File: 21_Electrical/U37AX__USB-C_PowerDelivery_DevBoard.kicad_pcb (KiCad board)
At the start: 2 copper layers, 96.6 x 80 mm, 93 parts, among them J1 USB_C_Receptacle_USB2.0_16P, J2 USB 2.0 OUT, J3 SWD1, J5 PD VBUS, J6 PD GND, J7 PD OUTPUT, J8 Conn_01x07_Pin, J9 Conn_02x04_Odd_Even, SW1 BTN, SW2 BOOT0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

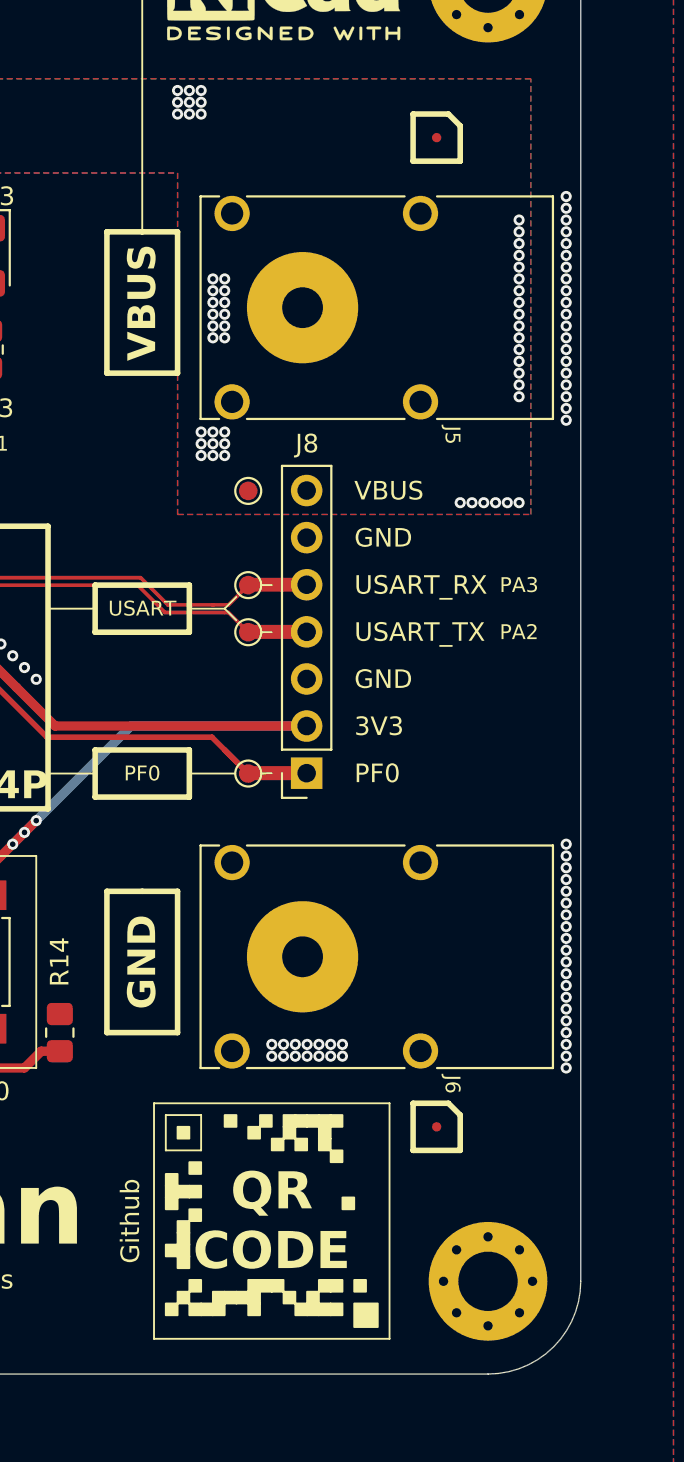
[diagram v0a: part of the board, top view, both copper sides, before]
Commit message: Qr_Code creation, Qr_Code footprint creation, adding Qr_Code to the PCB project
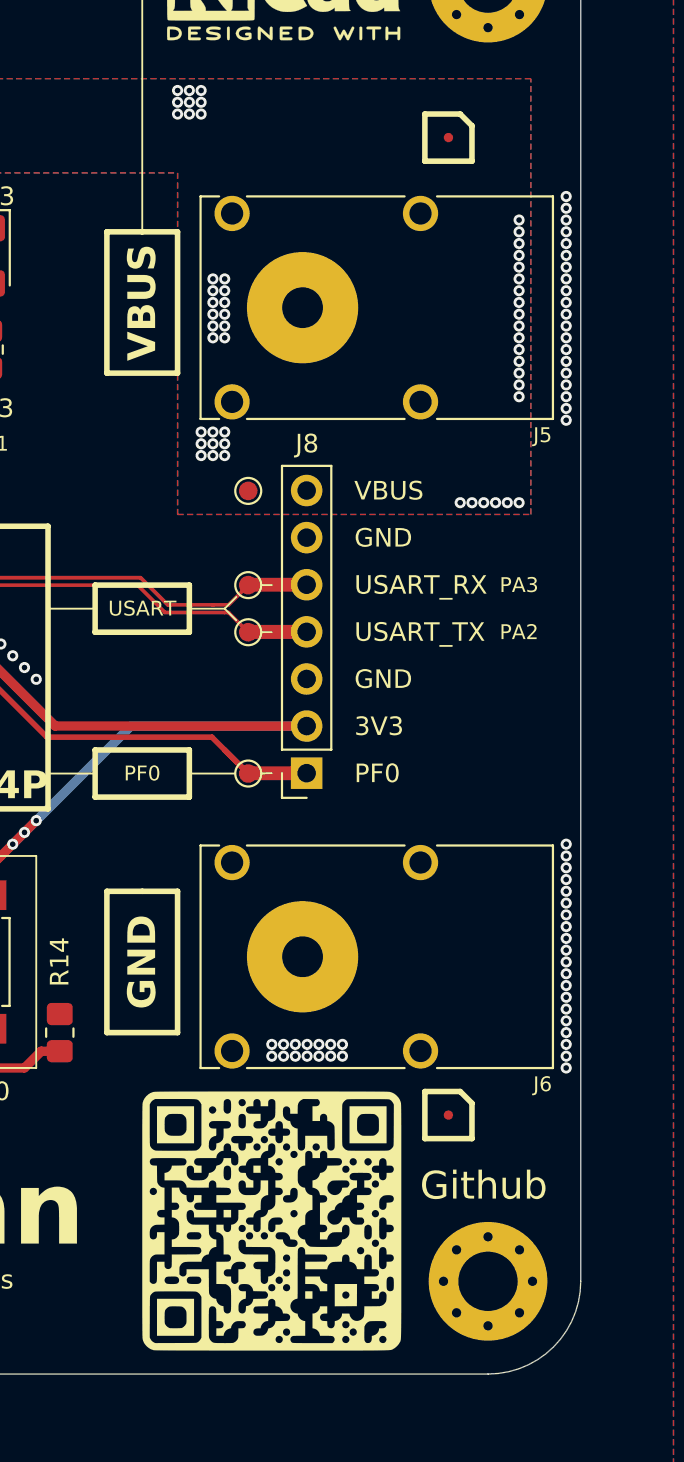
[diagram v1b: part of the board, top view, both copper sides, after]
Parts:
- added Github: LOGO, _URL_QrCode:URL_QrCode_0.55x0.55in, F.Cu at (189.9, 108.0)
- added Github: LOGO, _URL_QrCode:URL_QrCode_1.00x1.00in, B.Cu at (167.1, 101.6)
- moved FID1 0.90 mm to (199.5, 102.2)
- moved FID3 0.63 mm to (199.5, 49.5)
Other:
- board text removed: "Github"
- board text removed: "QR CODE"
